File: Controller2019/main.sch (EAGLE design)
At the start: 94 parts, among them Q1 IPT007N06N, Q2 IPT007N06N, Q3 IPT007N06N, Q4 IPT007N06N, Q5 IPT007N06N, Q6 IPT007N06N, U1 TEENSY_3.0+4, U2 DRV8301

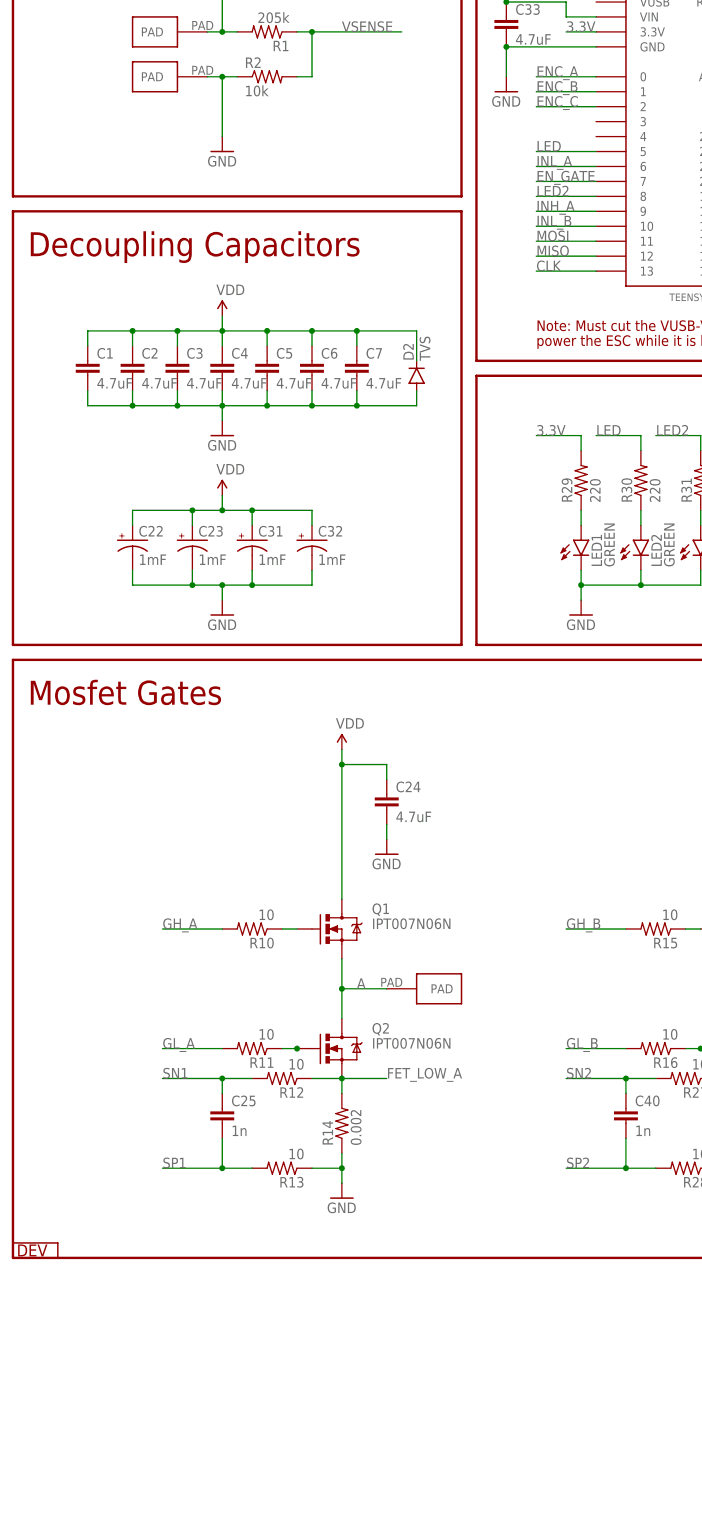
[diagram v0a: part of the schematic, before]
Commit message: Added CAN Transceiver
Added CAN Transceiver to 2019 Motor Controller. Did not update board
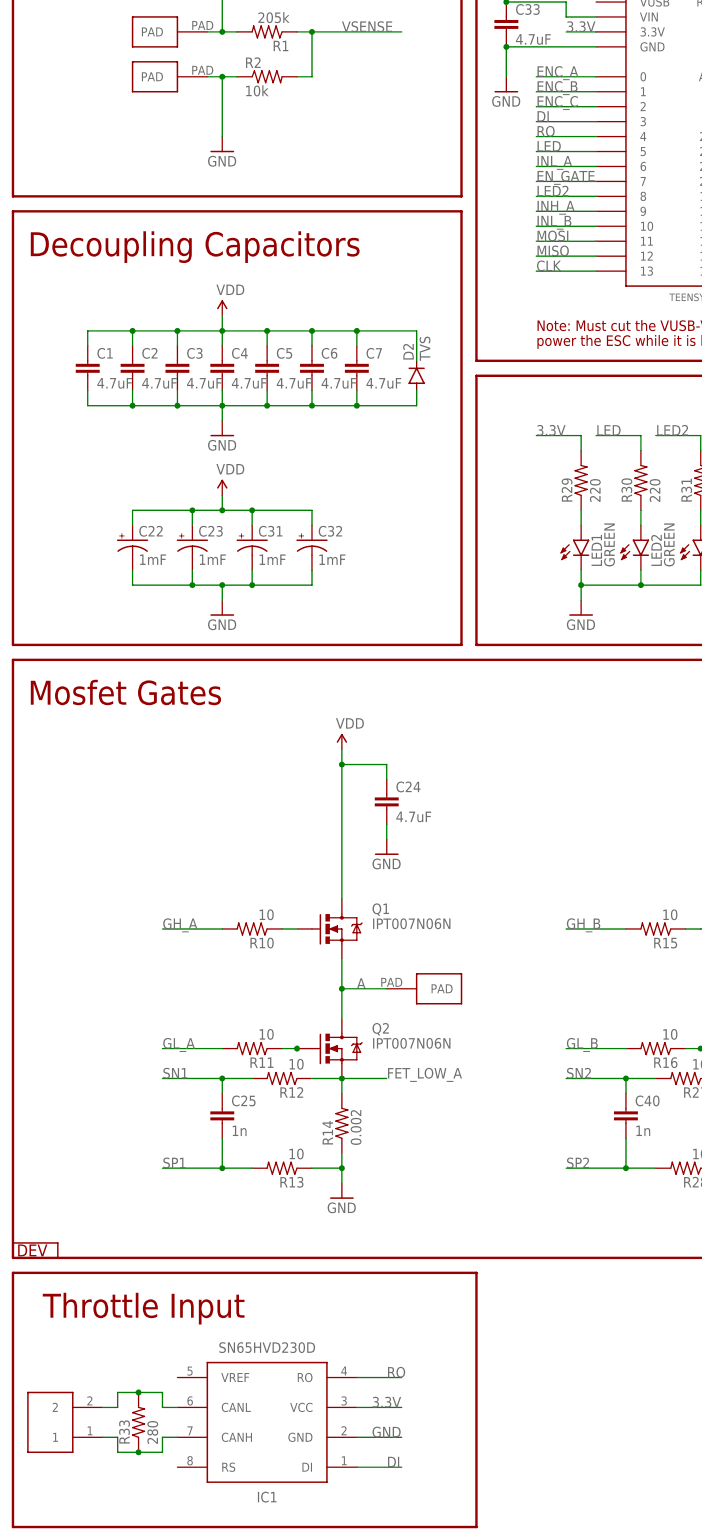
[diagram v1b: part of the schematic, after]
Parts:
- added IC1: SN65HVD230D, Misaka-IC:SN65HVD230D
- added R33: 280, SparkFun-Resistors:RESISTOR2512
- added U$29: HEADER2, Custom_old:HEADER2
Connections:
- new net DI: IC1.DI, U1.3
- new net N$18: IC1.CANL, R33.2, U$29.2
- new net N$19: IC1.CANH, R33.1, U$29.1
- new net RO: IC1.RO, U1.4
- net 3.3V: now also IC1.VCC
- net GND: now also IC1.GND
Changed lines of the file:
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@@
 <layer number="56" name="wert" color="7" fill="1" visible="no" active="no"/>
 <layer number="57" name="tCAD" color="7" fill="1" visible="no" active="no"/>
+<layer number="59" name="tCarbon" color="7" fill="1" visible="no" active="no"/>
+<layer number="60" name="bCarbon" color="7" fill="1" visible="no" active="no"/>
+<layer number="88" name="SimResults" color="9" fill="1" visible="yes" active="yes"/>
+<layer number="89" name="SimProbes" color="9" fill="1" visible="yes" active="yes"/>
 <layer number="90" name="Modules" color="5" fill="1" visible="yes" active="yes"/>
 <layer number="91" name="Nets" color="2" fill="1" visible="yes" active="yes"/>
@@
 <layer number="112" name="tSilk" color="7" fill="1" visible="no" active="yes"/>
 <layer number="113" name="IDFDebug" color="4" fill="1" visible="no" active="yes"/>
+<layer number="114" name="Badge_Outline" color="7" fill="1" visible="no" active="no"/>
+<layer number="115" name="ReferenceISLANDS" color="7" fill="1" visible="no" active="no"/>
 <layer number="116" name="Patch_BOT" color="9" fill="4" visible="yes" active="yes"/>
 <layer number="118" name="Rect_Pads" color="7" fill="1" visible="no" active="no"/>
@@
 <layer number="127" name="_tValues" color="7" fill="1" visible="no" active="yes"/>
 <layer number="128" name="_bValues" color="7" fill="1" visible="no" active="yes"/>
+<layer number="129" name="Mask" color="7" fill="1" visible="no" active="no"/>
 <layer number="131" name="tAdjust" color="7" fill="1" visible="no" active="yes"/>
 <layer number="132" name="bAdjust" color="7" fill="1" visible="no" active="yes"/>
@@
 <layer number="223" name="223bmp" color="24" fill="1" visible="no" active="no"/>
 <layer number="224" name="224bmp" color="25" fill="1" visible="no" active="no"/>
+<layer number="225" name="225bmp" color="7" fill="1" visible="no" active="no"/>
+<layer number="226" name="226bmp" color="7" fill="1" visible="no" active="no"/>
+<layer number="227" name="227bmp" color="7" fill="1" visible="no" active="no"/>
+<layer number="228" name="228bmp" color="7" fill="1" visible="no" active="no"/>
+<layer number="229" name="229bmp" color="7" fill="1" visible="no" active="no"/>
+<layer number="230" name="230bmp" color="7" fill="1" visible="no" active="no"/>
 <layer number="231" name="Eagle3D_PG1" color="7" fill="1" visible="no" active="no"/>
 <layer number="232" name="Eagle3D_PG2" color="7" fill="1" visible="no" active="no"/>
@@
 <part name="C21" library="SparkFun-Capacitors" deviceset="CAP" device="1206" value="4.7uF"/>
 <part name="C33" library="SparkFun-Capacitors" deviceset="CAP" device="1206" value="4.7uF"/>
+<part name="IC1" library="Misaka-IC" deviceset="SN65HVD23*D" device="" technology="0"/>
+<part name="U$29" library="Custom_old" deviceset="HEADER2" device=""/>
+<part name="R33" library="SparkFun-Resistors" deviceset="RESISTOR" device="2512" value="280"/>
 </parts>
 <sheets>
@@
 <wire x1="292.1" y1="0" x2="292.1" y2="43.18" width="0.4064" layer="94"/>
 <text x="241.3" y="35.56" size="3.81" layer="94">I2C Header</text>
+<wire x1="78.74" y1="-2.54" x2="0" y2="-2.54" width="0.4064" layer="94"/>
+<wire x1="0" y1="-45.72" x2="78.74" y2="-45.72" width="0.4064" layer="94"/>
+<wire x1="78.74" y1="-45.72" x2="78.74" y2="-2.54" width="0.4064" layer="94"/>
+<text x="5.08" y="-10.16" size="4.064" layer="94" distance="49">Throttle Input</text>
+<wire x1="0" y1="-45.72" x2="0" y2="-2.54" width="0.4064" layer="94"/>
 </plain>
 <instances>
@@
 <attribute name="NAME" x="85.344" y="211.201" size="1.778" layer="95"/>
 <attribute name="VALUE" x="85.344" y="206.121" size="1.778" layer="96"/>
+</instance>
+<instance part="IC1" gate="G$1" x="43.18" y="-27.94" rot="R180">
+<attribute name="NAME" x="43.18" y="-40.64" size="1.778" layer="95" rot="R180" align="center"/>
+<attribute name="VALUE" x="43.18" y="-15.24" size="1.778" layer="96" rot="R180" align="center"/>
+</instance>
+<instance part="U$29" gate="G$1" x="7.62" y="-25.4" rot="R180"/>
+<instance part="R33" gate="G$1" x="21.336" y="-27.94" rot="R90">
+<attribute name="NAME" x="19.8374" y="-31.75" size="1.778" layer="95" rot="R90"/>
+<attribute name="VALUE" x="24.638" y="-31.75" size="1.778" layer="96" rot="R90"/>
 </instance>
 </instances>
@@
 <wire x1="193.04" y1="17.78" x2="193.04" y2="15.24" width="0.1524" layer="91"/>
 </segment>
+<segment>
+<pinref part="IC1" gate="G$1" pin="GND"/>
+<wire x1="58.42" y1="-30.48" x2="66.04" y2="-30.48" width="0.1524" layer="91"/>
+<label x="60.96" y="-30.48" size="1.778" layer="95"/>
+</segment>
 </net>
 <net name="INH_A" class="0">
@@
 <label x="88.9" y="139.7" size="1.778" layer="95"/>
 </segment>
+<segment>
+<pinref part="IC1" gate="G$1" pin="VCC"/>
+<wire x1="58.42" y1="-25.4" x2="66.04" y2="-25.4" width="0.1524" layer="91"/>
+<label x="60.96" y="-25.4" size="1.778" layer="95"/>
+</segment>
 </net>
 <net name="N$13" class="0">
@@
 </segment>
 </net>
+<net name="N$18" class="0">
+<segment>
+<pinref part="IC1" gate="G$1" pin="CANL"/>
+<wire x1="27.94" y1="-25.4" x2="25.4" y2="-25.4" width="0.1524" layer="91"/>
+<wire x1="25.4" y1="-25.4" x2="25.4" y2="-22.86" width="0.1524" layer="91"/>
+<pinref part="R33" gate="G$1" pin="2"/>
+<wire x1="25.4" y1="-22.86" x2="21.336" y2="-22.86" width="0.1524" layer="91"/>
+<wire x1="21.336" y1="-22.86" x2="17.78" y2="-22.86" width="0.1524" layer="91"/>
+<junction x="21.336" y="-22.86"/>
+<wire x1="17.78" y1="-22.86" x2="17.78" y2="-25.4" width="0.1524" layer="91"/>
+<pinref part="U$29" gate="G$1" pin="2"/>
+<wire x1="17.78" y1="-25.4" x2="15.24" y2="-25.4" width="0.1524" layer="91"/>
+</segment>
+</net>
+<net name="N$19" class="0">
+<segment>
+<pinref part="U$29" gate="G$1" pin="1"/>
+<wire x1="15.24" y1="-30.48" x2="17.78" y2="-30.48" width="0.1524" layer="91"/>
+<wire x1="17.78" y1="-30.48" x2="17.78" y2="-33.02" width="0.1524" layer="91"/>
+<pinref part="R33" gate="G$1" pin="1"/>
+<wire x1="17.78" y1="-33.02" x2="21.336" y2="-33.02" width="0.1524" layer="91"/>
+<wire x1="21.336" y1="-33.02" x2="25.4" y2="-33.02" width="0.1524" layer="91"/>
+<junction x="21.336" y="-33.02"/>
+<wire x1="25.4" y1="-33.02" x2="25.4" y2="-30.48" width="0.1524" layer="91"/>
+<pinref part="IC1" gate="G$1" pin="CANH"/>
+<wire x1="25.4" y1="-30.48" x2="27.94" y2="-30.48" width="0.1524" layer="91"/>
+</segment>
+</net>
+<net name="RO" class="0">
+<segment>
+<pinref part="IC1" gate="G$1" pin="RO"/>
+<wire x1="58.42" y1="-20.32" x2="66.04" y2="-20.32" width="0.1524" layer="91"/>
+<label x="63.5" y="-20.32" size="1.778" layer="95"/>
+</segment>
+<segment>
+<pinref part="U1" gate="G$1" pin="4"/>
+<wire x1="99.06" y1="190.5" x2="88.9" y2="190.5" width="0.1524" layer="91"/>
+<label x="88.9" y="190.5" size="1.778" layer="95"/>
+</segment>
+</net>
+<net name="DI" class="0">
+<segment>
+<pinref part="IC1" gate="G$1" pin="DI"/>
+<wire x1="58.42" y1="-35.56" x2="66.04" y2="-35.56" width="0.1524" layer="91"/>
+<label x="63.5" y="-35.56" size="1.778" layer="95"/>
+</segment>
+<segment>
+<pinref part="U1" gate="G$1" pin="3"/>
+<wire x1="99.06" y1="193.04" x2="88.9" y2="193.04" width="0.1524" layer="91"/>
+<label x="88.9" y="193.04" size="1.778" layer="95"/>
+</segment>
+</net>

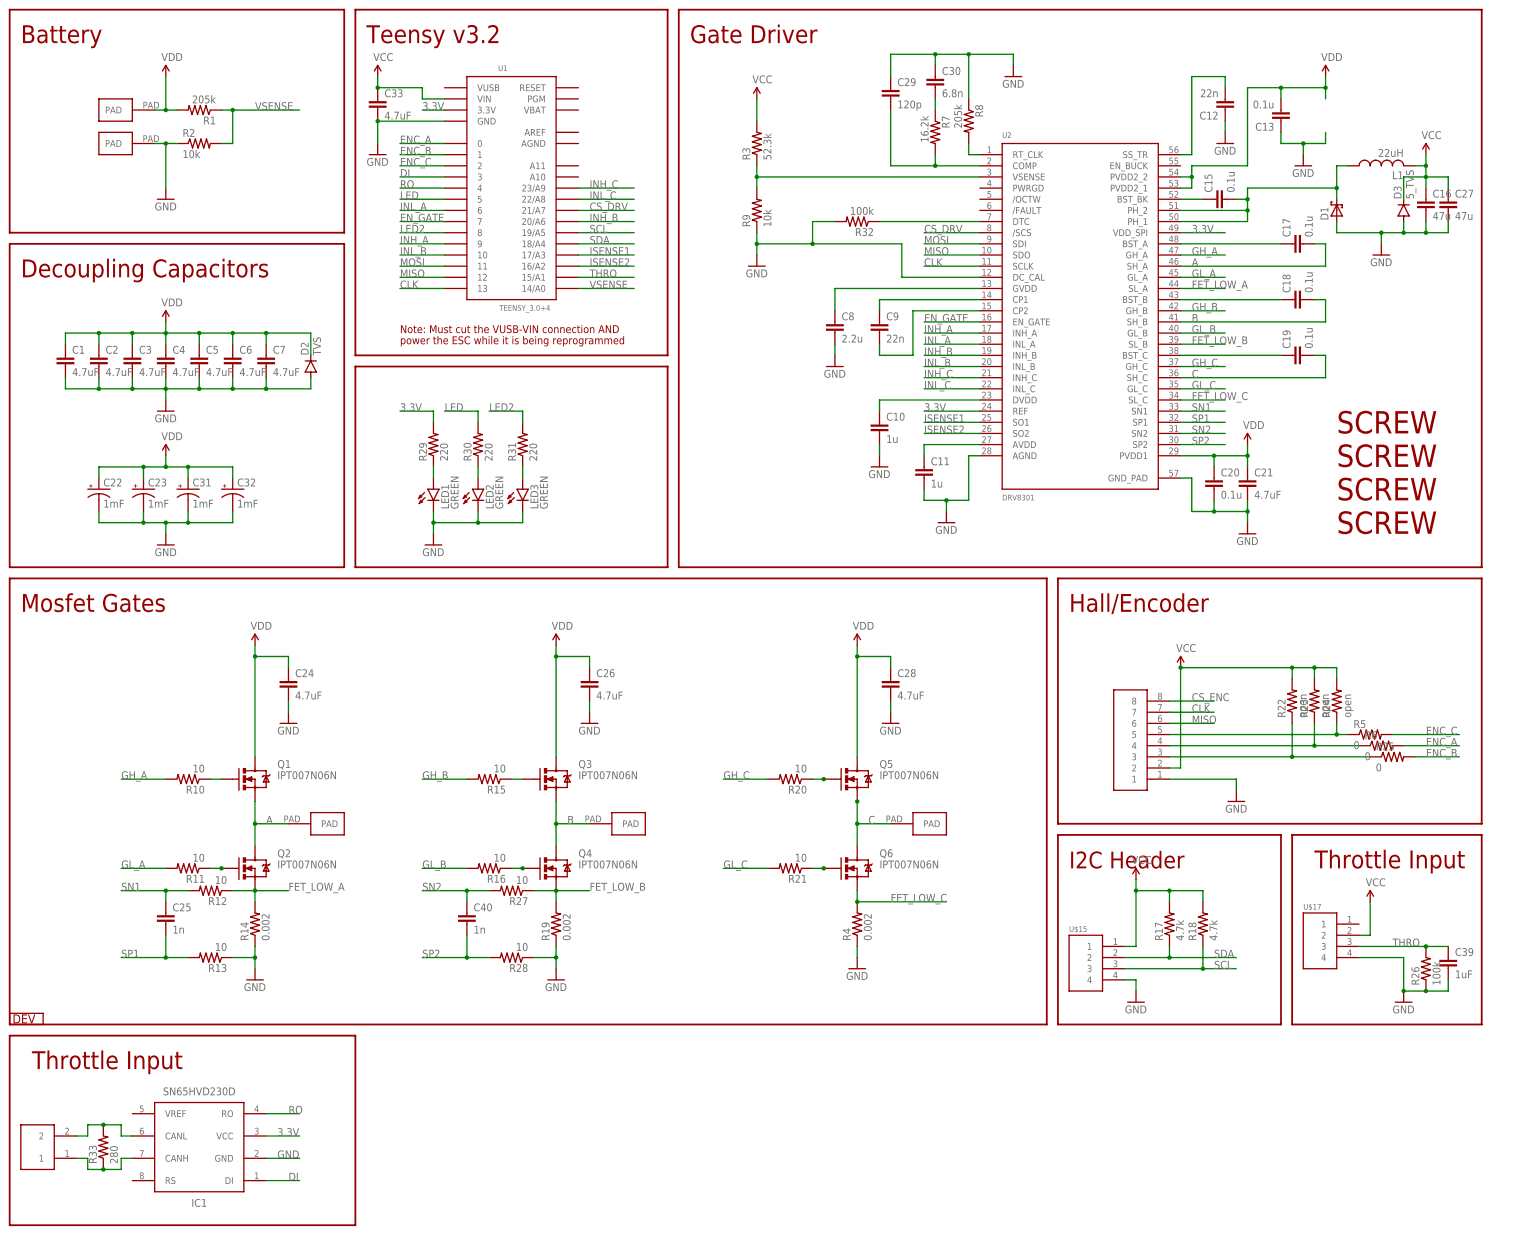
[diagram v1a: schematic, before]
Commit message: route fixes, routed CAN transciever
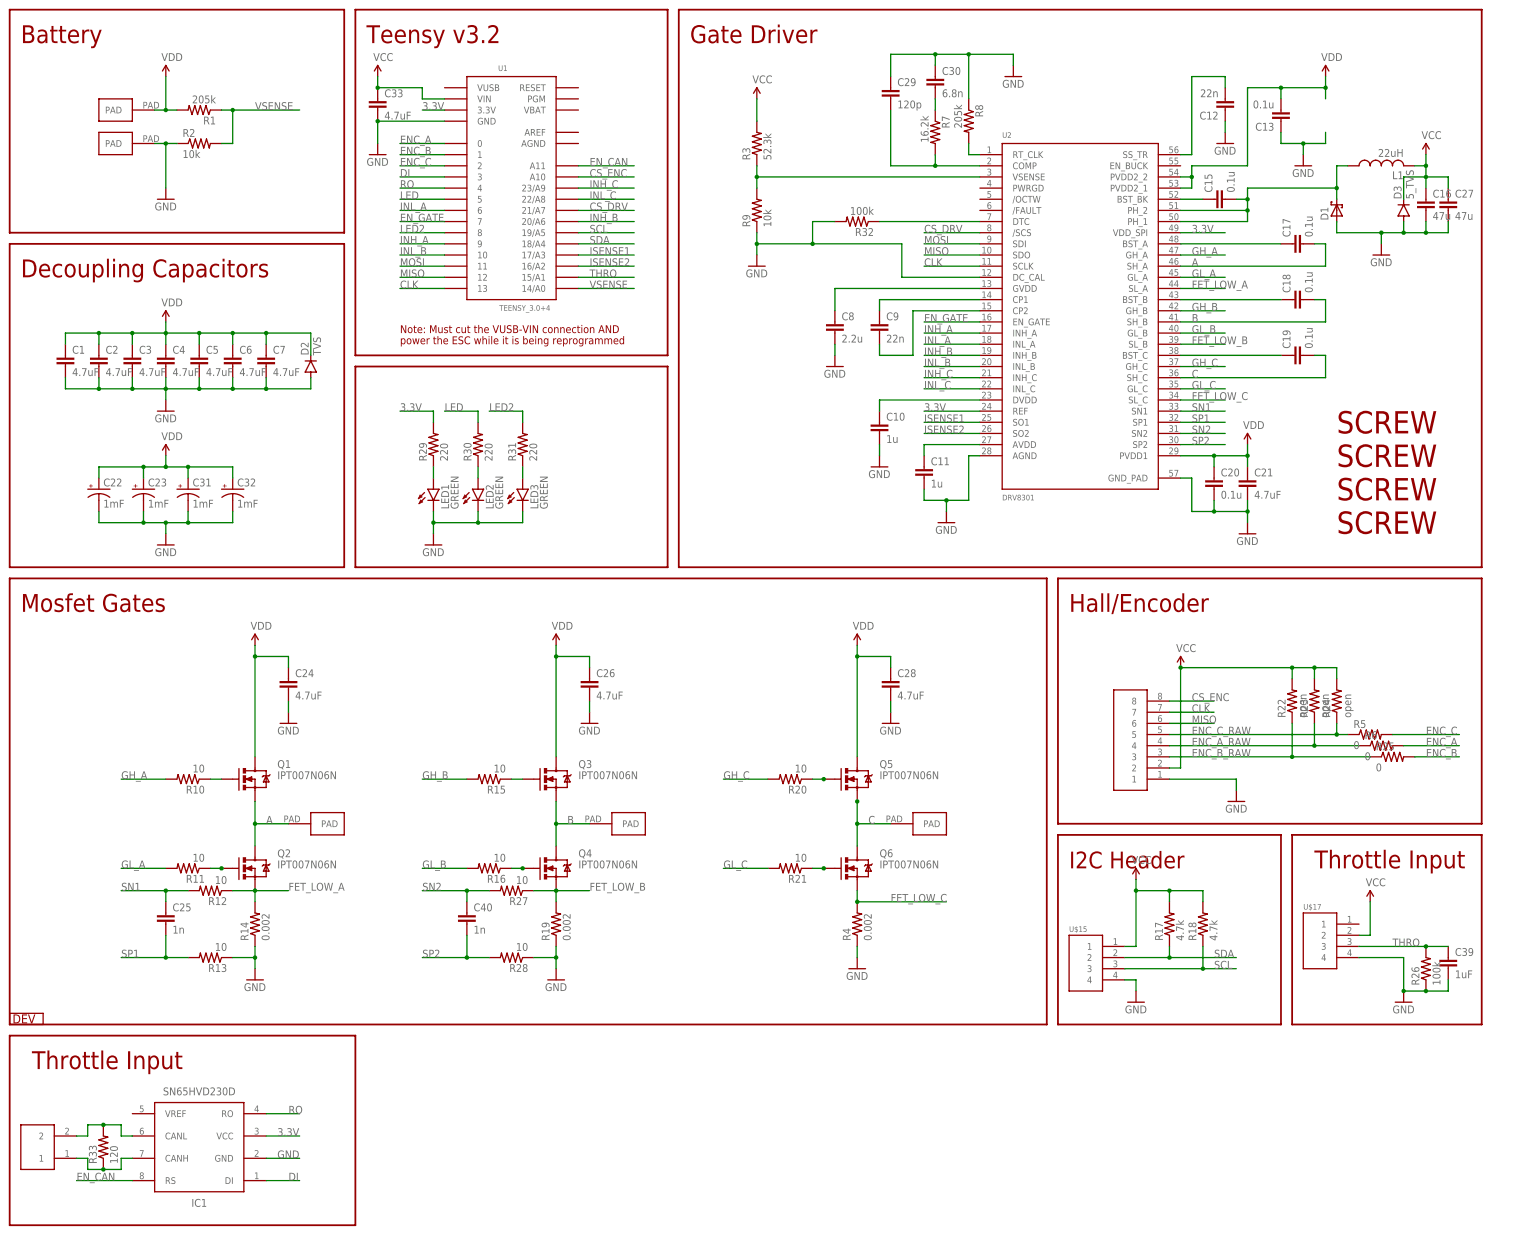
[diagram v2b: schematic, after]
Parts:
- C12, C13, C15, C17, C18, C19, C20, C25, C29, C30, C40, C8, C9: device SparkFun-Capacitors:CAP0603-CAP -> SparkFun-Passives:CAP0603-CAP
- R1, R10, R11, R12, R13, R15, R16, R2, R20, R21, R22, R23, R24, R27, R28, R29, R3, R30, R31, R32, R7, R8, R9: device SparkFun-Resistors:RESISTOR0603 -> SparkFun-Passives:RESISTOR0603-RES
- R33: value 280 -> 120; device SparkFun-Resistors:RESISTOR2512 -> SparkFun-Passives:RESISTOR0603-RES
- renumbered U$29 to CAN
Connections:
- net N$13 renamed ENC_C_RAW
- net N$14 renamed ENC_A_RAW
- net N$15 renamed ENC_B_RAW
- net N$18 renamed CANL
- net N$19 renamed CANH
- new net EN_CAN: IC1.RS, U1.A11
- net CS_ENC: now also U1.A10
